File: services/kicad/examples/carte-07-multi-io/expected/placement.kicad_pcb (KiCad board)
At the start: 2 copper layers, 110 x 80 mm, 44 parts, among them J1 IN_5V, J10 IO0, J11 IO1, J12 IO2, J2 SWD, U1 STM32F103C8T6, U2 AMS1117-3.3

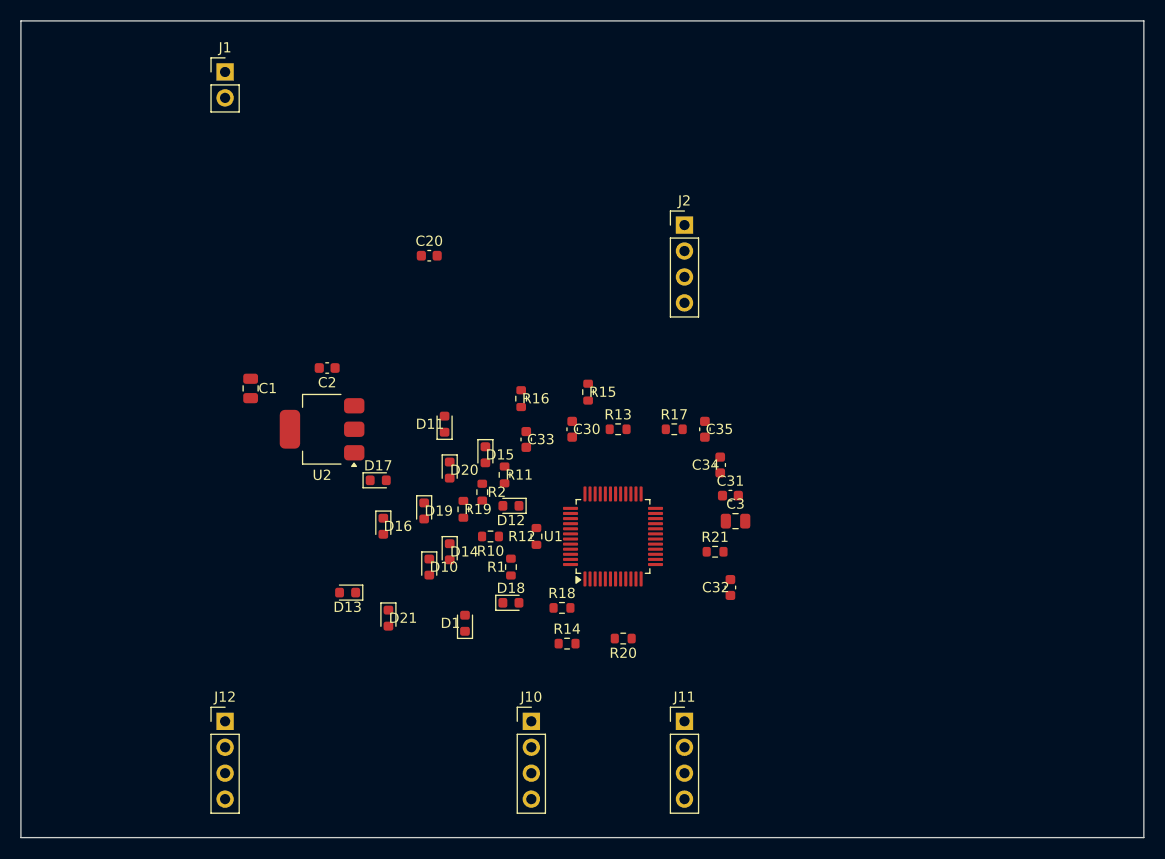
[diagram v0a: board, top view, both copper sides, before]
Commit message: feat(examples): carte-07 livree -- 100 %, 0 erreur, 2 couches, decouplage 2,5 mm, paires 2,5 mm, grille 91 %
Placement complet (contrainte de decouplage + rangees LED/R + une capa par broche VDD), tirage de preuve sous le plancher. Placement livre a cote du board route.

Co-Authored-By: Claude Fable 5.1 <noreply@anthropic.com>

Claude-Session: https://claude.ai/code/session_01TnMqm4La2CxQHHB5K8aSSV
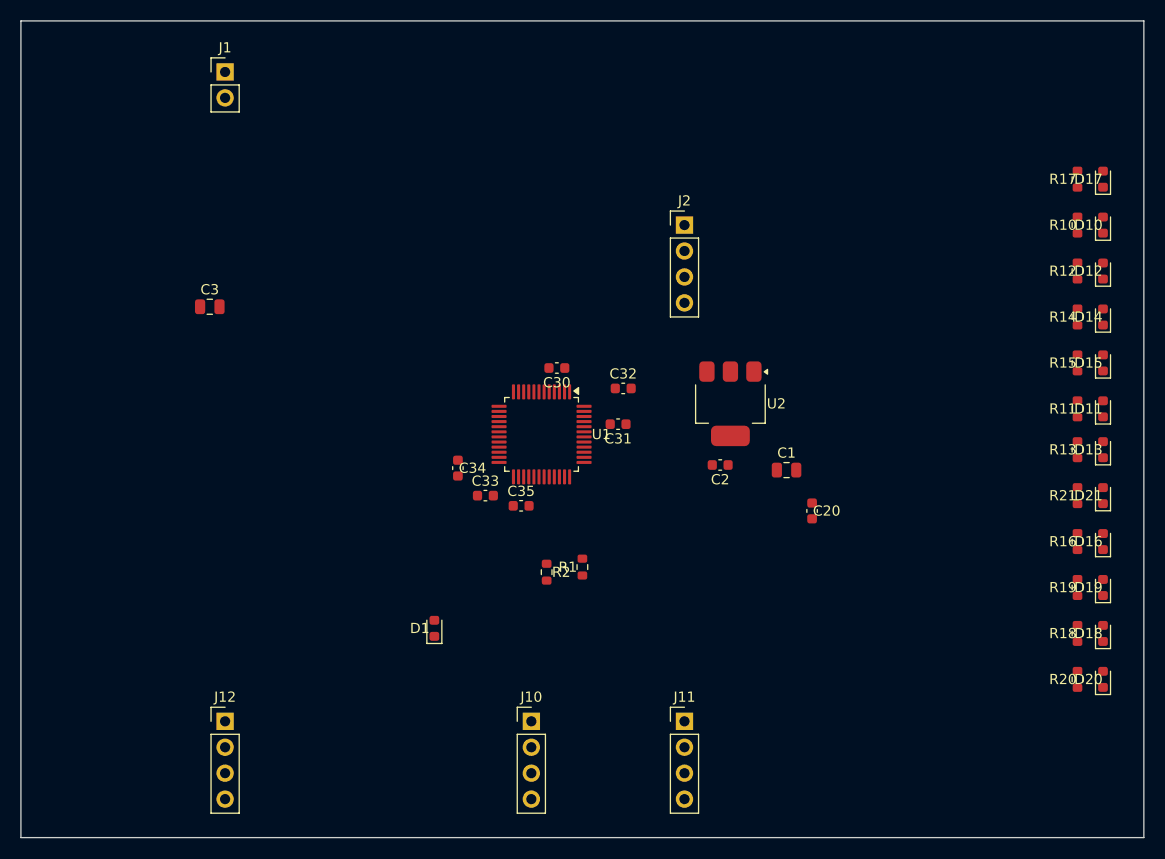
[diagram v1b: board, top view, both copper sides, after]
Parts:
- moved D17 76.9 mm to (199.5, 80.5), turned to 90 degrees
- moved D13 75.3 mm to (199.5, 107.0), turned to 90 degrees
- moved D10 74.0 mm to (199.5, 85.0), turned to 90 degrees
- moved D21 71.0 mm to (199.5, 111.5), turned to 90 degrees
- moved D16 70.5 mm to (199.5, 116.0), turned to 90 degrees
- moved D14 68.0 mm to (199.5, 94.0), turned to 90 degrees
- moved D20 67.2 mm to (199.5, 129.5), turned to 90 degrees
- moved D19 66.9 mm to (199.5, 120.5), turned to 90 degrees
- moved R10 65.1 mm to (197.0, 85.0), turned to 90 degrees
- moved D11 64.5 mm to (199.5, 103.0)
- moved D12 62.4 mm to (199.5, 89.5), turned to 90 degrees
- moved D15 61.2 mm to (199.5, 98.5), turned to 90 degrees
- moved R19 60.6 mm to (197.0, 120.5), turned to 90 degrees
- moved R14 59.4 mm to (197.0, 94.0), turned to 90 degrees
- moved R12 59.0 mm to (197.0, 89.5)
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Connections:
- C3 pad 1: +3V3 -> Net-(C3-1)
- U1 pad 36: +3V3 -> Net-(U1-36)
- U1 pad 48: +3V3 -> Net-(U1-48)
- U2 pad 2: +3V3 -> Net-(U2-2)

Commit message: examples: carte-01 a 07 -- placement valide et gele (phase 1) puis route dessus (phase 2) : 100 %, 0 erreur, 2 couches
Sequence en deux phases demandee par l'utilisateur : valider_placements.py (critere pro : chaque broche VDD a sa capa a <= 3,5 mm) puis banc_exemples.py --placement-fige. 30 s a 2,6 min de routage par carte.

Co-Authored-By: Claude Fable 5.1 <noreply@anthropic.com>

Claude-Session: https://claude.ai/code/session_01TnMqm4La2CxQHHB5K8aSSV
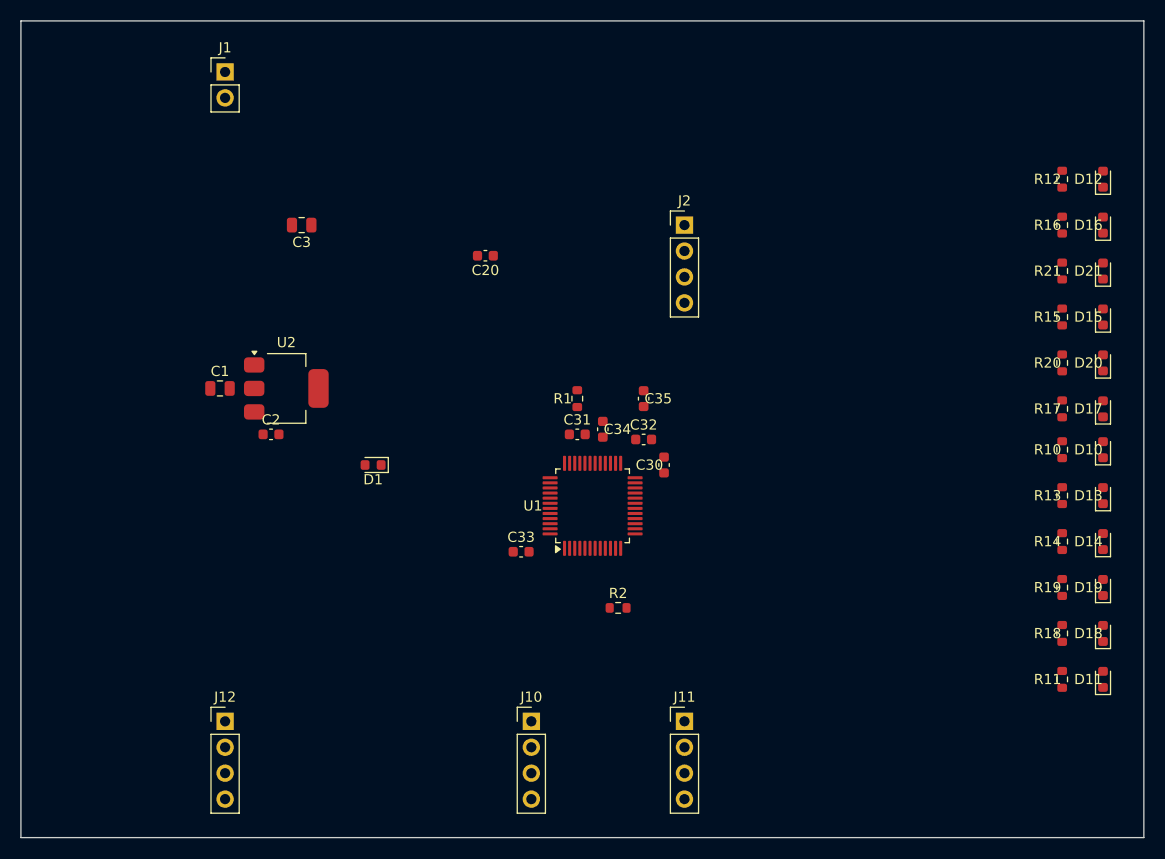
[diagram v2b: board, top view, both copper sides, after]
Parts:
- moved C1 56.1 mm to (113.0, 101.0)
- moved C2 44.1 mm to (118.0, 105.5), turned to 0 degrees
- moved U2 43.5 mm to (119.5, 101.0), turned to 0 degrees
- moved C20 40.6 mm to (139.0, 88.0), turned to 180 degrees
- moved R16 31.0 mm to (195.5, 85.0)
- moved R20 31.0 mm to (195.5, 98.5)
- moved D16 31.0 mm to (199.5, 85.0)
- moved D20 31.0 mm to (199.5, 98.5)
- moved R11 26.5 mm to (195.5, 129.5)
- moved D11 26.5 mm to (199.5, 129.5)
- moved R17 22.5 mm to (195.5, 103.0)
- moved D17 22.5 mm to (199.5, 103.0)
- moved R10 22.1 mm to (195.5, 107.0)
- moved R14 22.1 mm to (195.5, 116.0)
- moved R21 22.1 mm to (195.5, 89.5)
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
